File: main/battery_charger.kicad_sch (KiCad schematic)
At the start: 52 parts, among them Q1601 IXTP28P065T, Q1602 TK4R3E06PL, Q1603 IRLML0030, Q1604 FDS6681Z, Q1605 FDS6681Z, Q1606 IRLML0030, U1601 LT8710, U1602 TMCS1101, U1603 TSV911xxLx

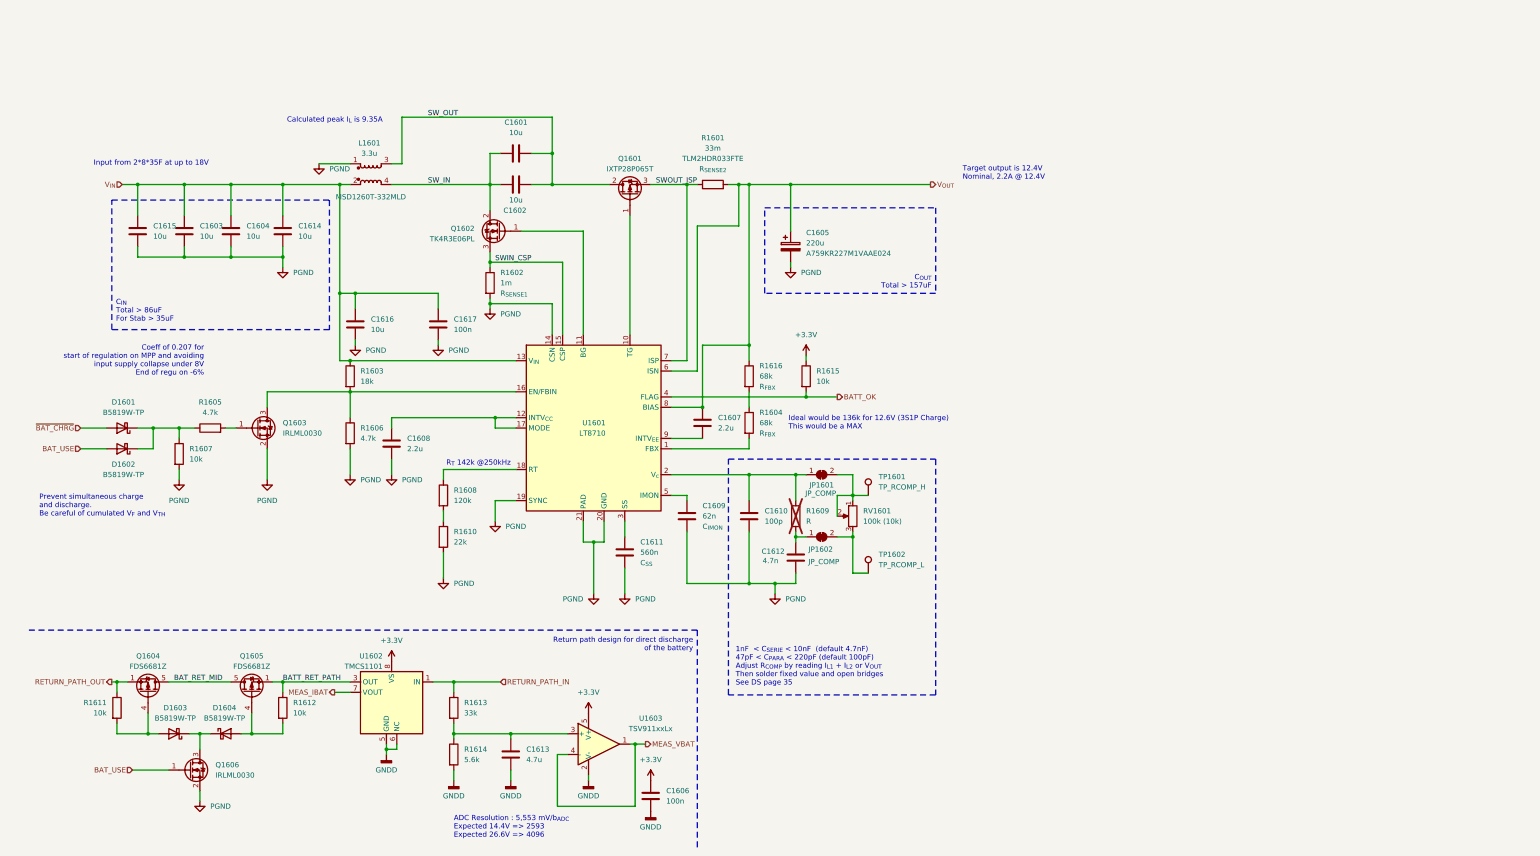
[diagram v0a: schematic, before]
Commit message: Clean silkscreen
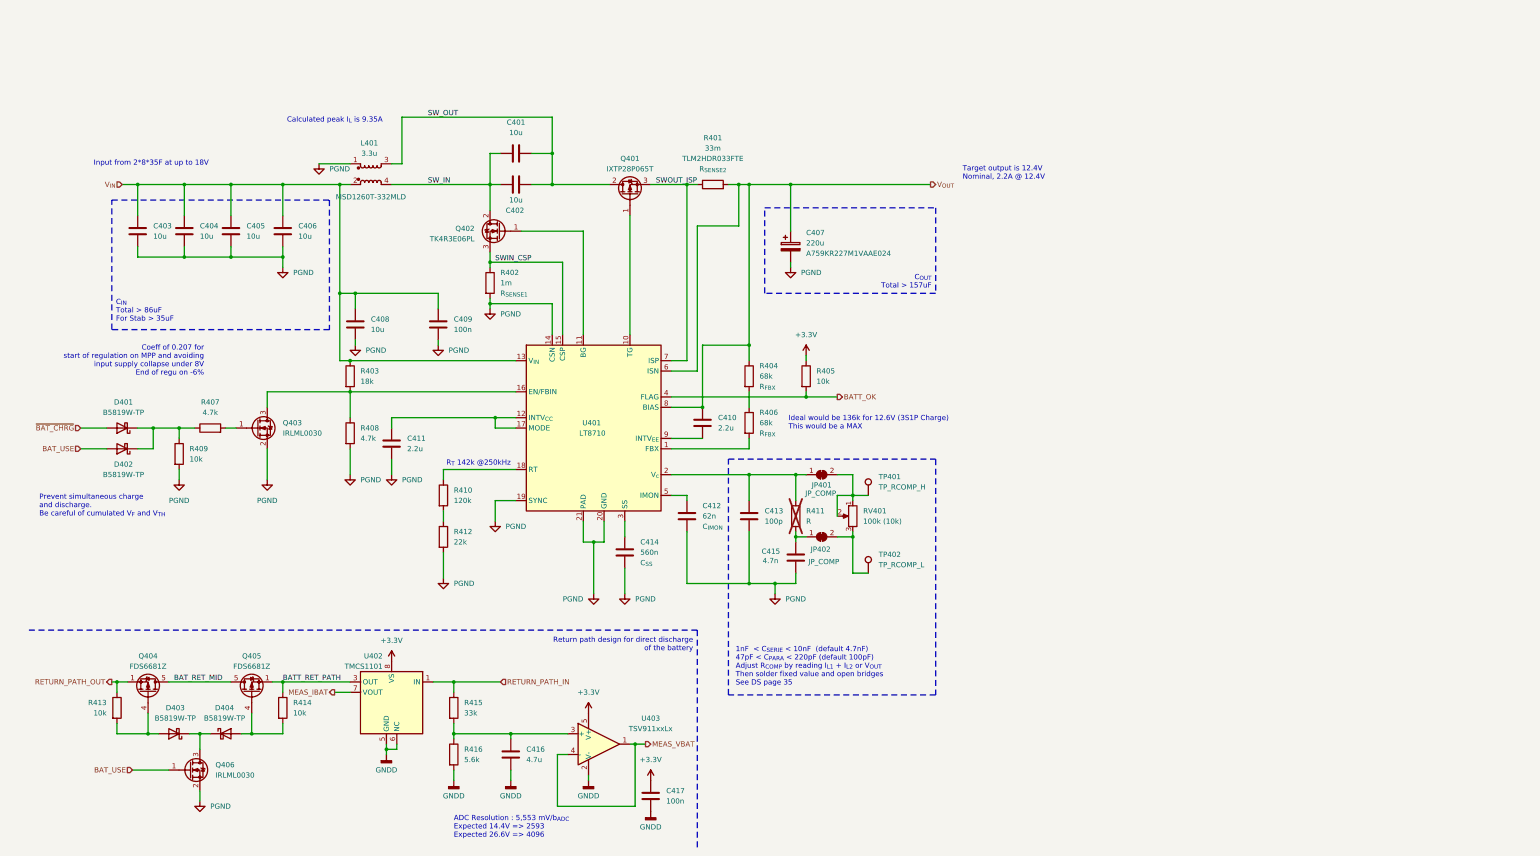
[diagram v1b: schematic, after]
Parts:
- renumbered C1601 to C401, C1602 to C402, C1615 to C403, C1603 to C404, C1604 to C405, C1614 to C406, C1605 to C407, C1616 to C408, C1617 to C409, C1607 to C410, C1608 to C411, C1609 to C412, C1610 to C413, C1611 to C414, C1612 to C415, C1613 to C416, C1606 to C417, D1601 to D401, D1602 to D402, D1603 to D403, D1604 to D404, JP1601 to JP401, JP1602 to JP402, L1601 to L401, Q1601 to Q401, Q1602 to Q402, Q1603 to Q403, Q1604 to Q404, Q1605 to Q405, Q1606 to Q406, R1601 to R401, R1602 to R402, R1603 to R403, R1616 to R404, R1615 to R405, R1604 to R406, R1605 to R407, R1606 to R408, R1607 to R409, R1608 to R410, R1609 to R411, R1610 to R412, R1611 to R413, R1612 to R414, R1613 to R415, R1614 to R416, RV1601 to RV401, TP1601 to TP401, TP1602 to TP402, U1601 to U401, U1602 to U402, U1603 to U403

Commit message: Sent to fab
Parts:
- C401, C402, C403, C404, C405, C406, C408: MPN (none) -> CL21A106KBYQNNE; Mouser SKU (none) -> 187-CL21A106KBYQNNE
- C407: Mouser SKU (none) -> 80-A759KR227M1VAAE24
- C409, C417: MPN (none) -> CL21B104KACNFNC; Mouser SKU (none) -> 187-CL21B104KACNFNC
- C410, C411: MPN (none) -> CL21B225KBYNNWE; Mouser SKU (none) -> 187-CL21B225KBYNNWE
- C412: value 62n -> 68n; MPN (none) -> CL21B683KBCWPNC; Mouser SKU (none) -> 187-CL21B683KBCWPNC
- C413: MPN (none) -> CL21C101JBANNND; Mouser SKU (none) -> 187-CL21C101JBANNND
- C414: value 560n -> 680n; MPN (none) -> CL21B684JOFNNNE; Mouser SKU (none) -> 187-CL21B684JOFNNNE
- C415: MPN (none) -> CL21C472JAFNNNE; Mouser SKU (none) -> 187-CL21C472JAFNNNE
- C416: MPN (none) -> CL21B475KAFNNNE; Mouser SKU (none) -> 187-CL21B475KAFNNNE
- L401: Mouser SKU (none) -> 994-MSD1260T-332MLD
- R401: Mouser SKU (none) -> 279-TLM2HDR033FTE
- R402: MPN (none) -> WSL20101L000FEA18; Mouser SKU (none) -> 71-WSL20101L000FEA18

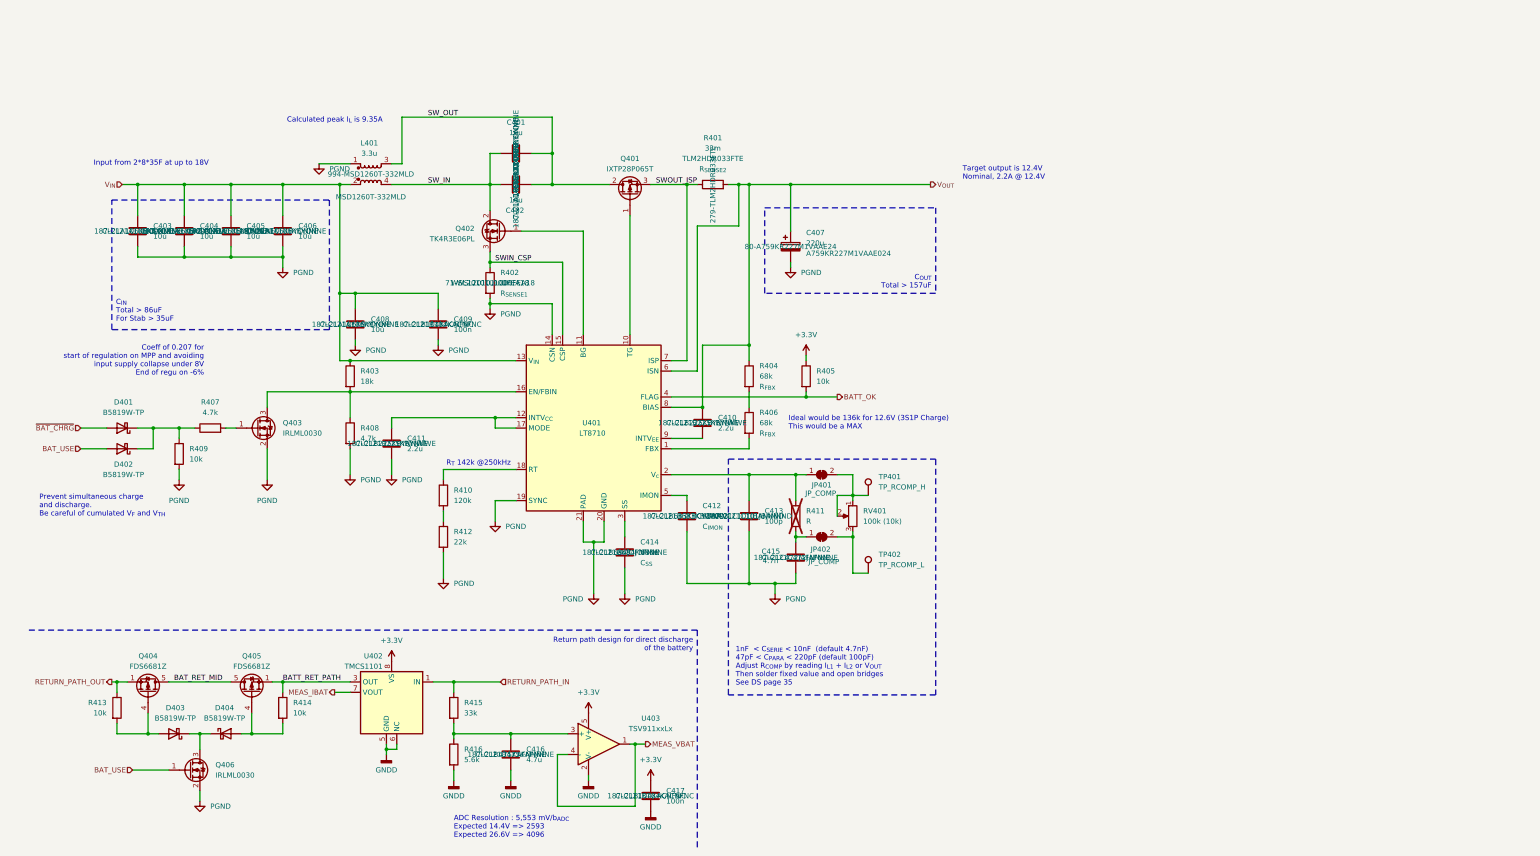
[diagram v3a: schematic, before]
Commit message: BOM almost OK, starts new side board.
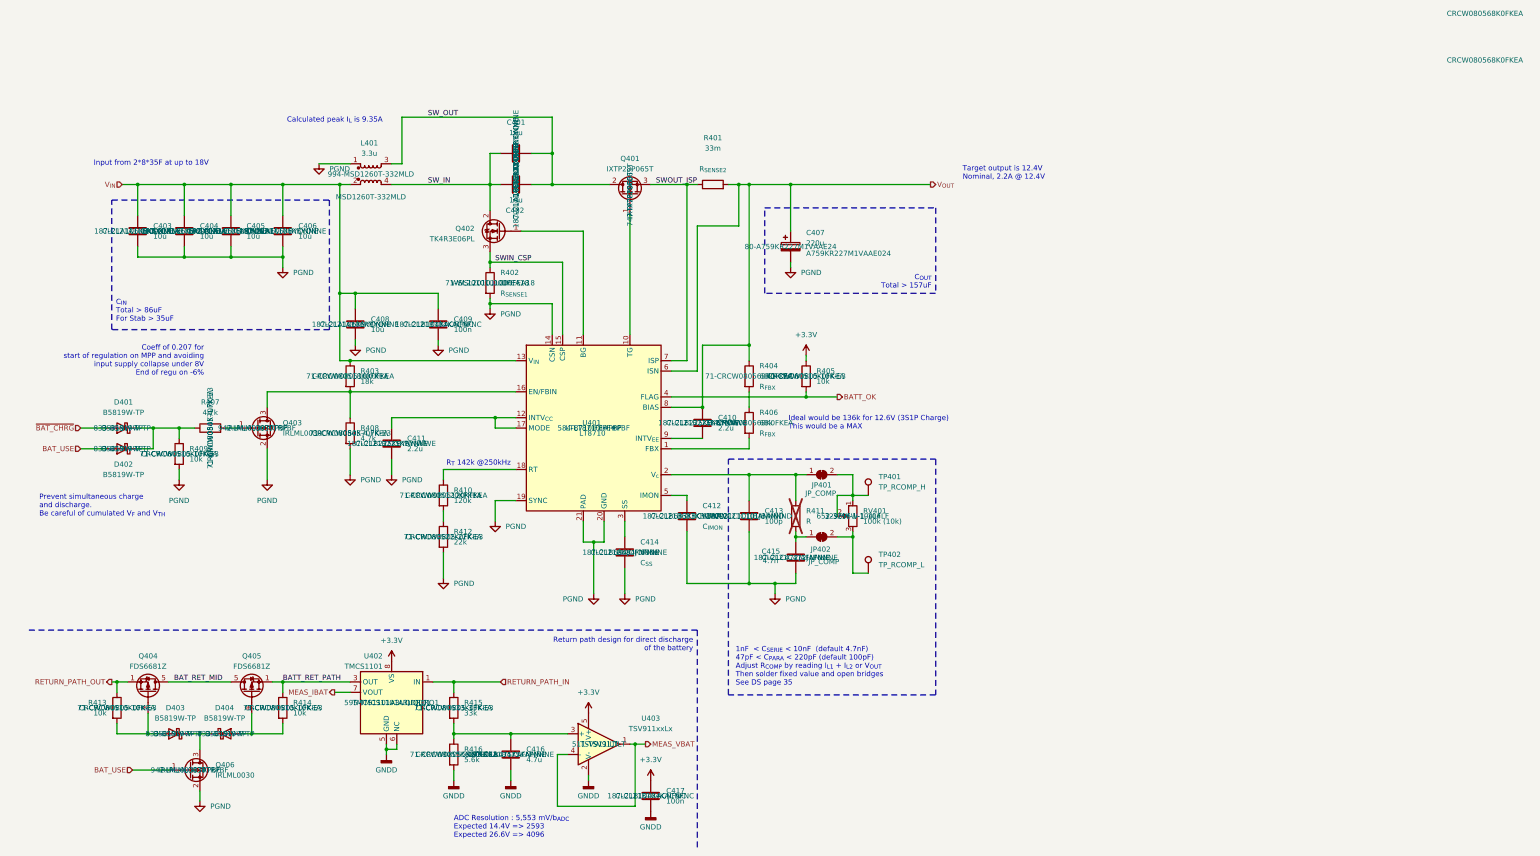
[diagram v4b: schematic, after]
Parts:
- D401, D402, D403, D404: MPN (none) -> B5819W-TP; Mouser SKU (none) -> 833-B5819W-TP
- JP401, JP402: now left out of the parts list
- Q401: MPN (none) -> IXTP28P065T; Mouser SKU (none) -> 747-IXTP28P065T
- Q403, Q406: MPN (none) -> IRLML0030TRPBF; Mouser SKU (none) -> 942-IRLML0030TRPBF
- R401: MPN TLM2HDR033FTE -> (none); Mouser SKU 279-TLM2HDR033FTE -> (none)
- R403: MPN (none) -> CRCW080518K0FKEA; Mouser SKU (none) -> 71-CRCW080518K0FKEA
- R404, R406: MPN (none) -> CRCW080568K0FKEA; Mouser SKU (none) -> 71-CRCW080568K0FKEA
- R405, R409, R413, R414: MPN (none) -> CRCW080510K0FKEA; Mouser SKU (none) -> 71-CRCW0805-10K-E3
- R407, R408: MPN (none) -> CRCW08054K70FKEA; Mouser SKU (none) -> 71-CRCW0805-4.7K-E3
- R410: MPN (none) -> CRCW0805120KFKEA; Mouser SKU (none) -> 71-CRCW0805120KFKEA
- R412: MPN (none) -> CRCW080522K0FKEA; Mouser SKU (none) -> 71-CRCW0805-22K-E3
- R415: MPN (none) -> CRCW080533K0FKEA; Mouser SKU (none) -> 71-CRCW0805-33K-E3
- R416: MPN (none) -> CRCW08055K60FKEA; Mouser SKU (none) -> 71-CRCW08055K60FKEA
- RV401: MPN (none) -> 3296W-1-104LF; Mouser SKU (none) -> 652-3296W-1-104LF
- U401: MPN (none) -> LT8710IFE#PBF; Mouser SKU (none) -> 584-LT8710IFE#PBF
- U402: MPN (none) -> TMCS1101A3UQDRQ1; Mouser SKU (none) -> 595-TMCS1101A3UQDRQ1
- U403: MPN (none) -> TSV911ILT; Mouser SKU (none) -> 511-TSV911ILT

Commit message: Revised with BOM ordered
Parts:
- C401, C402, C403, C404, C405, C406, C408: Mouser SKU 187-CL21A106KBYQNNE -> 187-CL21A106KBYQNNE
- C407: Mouser SKU 80-A759KR227M1VAAE24 -> 80-A759KR227M1VAAE24
- C409, C417: Mouser SKU 187-CL21B104KACNFNC -> 187-CL21B104KACNFNC
- C410, C411: Mouser SKU 187-CL21B225KBYNNWE -> 187-CL21B225KBYNNWE
- C412: Mouser SKU 187-CL21B683KBCWPNC -> 187-CL21B683KBCWPNC
- C413: Mouser SKU 187-CL21C101JBANNND -> 187-CL21C101JBANNND
- C414: Mouser SKU 187-CL21B684JOFNNNE -> 187-CL21B684JOFNNNE
- C415: Mouser SKU 187-CL21C472JAFNNNE -> 187-CL21C472JAFNNNE
- C416: Mouser SKU 187-CL21B475KAFNNNE -> 187-CL21B475KAFNNNE
- L401: value 3.3u -> 4.7u; MPN MSD1260T-332MLD -> MSD1260T-472MLD; Mouser SKU 994-MSD1260T-332MLD -> 994-MSD1260T-472MLD
- Q404, Q405: MPN (none) -> FDS6681Z; Mouser SKU (none) -> 512-FDS6681Z
- R401: value 33m -> 18m; MPN (none) -> WSL2010R0180FEA; Mouser SKU (none) -> 71-WSL2010R0180FEA
- R402: value 1m -> 6m; Mouser SKU 71-WSL20101L000FEA18 -> 71-WSL20101L000FEA18
- R404, R406: MPN CRCW080568K0FKEA -> CRCW080568K0FKEAC; Mouser SKU 71-CRCW080568K0FKEA -> 71-CRCW080568K0FKEAC
- U401: MPN LT8710IFE#PBF -> LT8710IFE#PBF
- U402: MPN TMCS1101A3UQDRQ1 -> TMCS1101A3UQDRQ1
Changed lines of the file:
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@@
 			)
 		)
-		(property "Mouser SKU" " 187-CL21B684JOFNNNE "
+		(property "Mouser SKU" "187-CL21B684JOFNNNE "
 			(at 157.48 124.46 0)
 			(effects
@@
 			)
 		)
+		(property "MPN" "FDS6681Z"
+			(at 66.04 158.75 0)
+			(effects
+				(font
+					(size 1.27 1.27)
+				)
+			)
+		)
+		(property "Mouser SKU" "512-FDS6681Z "
+			(at 66.04 158.75 0)
+			(effects
+				(font
+					(size 1.27 1.27)
+				)
+			)
+		)
 		(pin "6"
 		)
@@
 			)
 		)
-		(property "Mouser SKU" " 187-CL21A106KBYQNNE "
+		(property "Mouser SKU" "187-CL21A106KBYQNNE "
 			(at 130.81 26.67 0)
 			(effects
@@
 			)
 		)
-		(property "Mouser SKU" " 187-CL21A106KBYQNNE "
+		(property "Mouser SKU" "187-CL21A106KBYQNNE "
 			(at 60.96 45.72 0)
 			(effects
@@
 			)
 		)
-		(property "Mouser SKU" " 187-CL21B225KBYNNWE "
+		(property "Mouser SKU" "187-CL21B225KBYNNWE "
 			(at 176.53 92.71 0)
 			(effects
@@
 			)
 		)
-		(property "Value" "3.3u"
+		(property "Value" "4.7u"
 			(at 94.869 26.67 0)
 			(effects
@@
 			)
 		)
-		(property "MPN" " MSD1260T-332MLD "
+		(property "MPN" "MSD1260T-472MLD"
 			(at 95.25 37.338 0)
 			(effects
@@
 			)
 		)
-		(property "Mouser SKU" " 994-MSD1260T-332MLD "
+		(property "Mouser SKU" "994-MSD1260T-472MLD"
+			(at 95.25 31.75 0)
+			(effects
+				(font
+					(size 1.27 1.27)
+				)
+			)
+		)
+		(property "Name" ""
 			(at 95.25 31.75 0)
 			(effects
@@
 		(fields_autoplaced yes)
 		(property "Reference" "R402"
-			(at 127 55.8799 0)
+			(at 127 53.3399 0)
 			(effects
 				(font
@@
 			)
 		)
-		(property "Value" "1m"
-			(at 127 58.4199 0)
+		(property "Value" "6m"
+			(at 127 55.8799 0)
 			(effects
 				(font
@@
 		)
 		(property "MPN" "WSL20101L000FEA18"
-			(at 124.46 58.42 0)
+			(at 127 58.4199 0)
 			(effects
 				(font
 					(size 1.27 1.27)
 				)
+				(justify left)
 			)
 		)
@@
 			)
 		)
-		(property "Mouser SKU" " 71-WSL20101L000FEA18 "
-			(at 124.46 58.42 0)
+		(property "Mouser SKU" "71-WSL20101L000FEA18 "
+			(at 127 63.4999 0)
 			(effects
 				(font
 					(size 1.27 1.27)
 				)
+				(justify left)
 			)
 		)
@@
 			)
 		)
-		(property "MPN" " LT8710IFE#PBF "
+		(property "MPN" "LT8710IFE#PBF "
 			(at 149.86 93.98 0)
 			(effects
@@
 			)
 		)
-		(property "Mouser SKU" " 187-CL21A106KBYQNNE "
+		(property "Mouser SKU" "187-CL21A106KBYQNNE "
 			(at 91.44 68.58 0)
 			(effects
@@
 			)
 		)
-		(property "Mouser SKU" " 187-CL21C101JBANNND "
+		(property "Mouser SKU" "187-CL21C101JBANNND "
 			(at 187.96 115.57 0)
 			(effects
@@
 			)
 		)
-		(property "Mouser SKU" " 187-CL21A106KBYQNNE "
+		(property "Mouser SKU" "187-CL21A106KBYQNNE "
 			(at 49.53 45.72 0)
 			(effects
@@
 			)
 		)
-		(property "Mouser SKU" " 187-CL21B683KBCWPNC "
+		(property "Mouser SKU" "187-CL21B683KBCWPNC "
 			(at 172.72 115.57 0)
 			(effects
@@
 			)
 		)
-		(property "Mouser SKU" " 187-CL21A106KBYQNNE "
+		(property "Mouser SKU" "187-CL21A106KBYQNNE "
 			(at 130.81 34.29 0)
 			(effects
@@
 			)
 		)
-		(property "Mouser SKU" " 187-CL21C472JAFNNNE "
+		(property "Mouser SKU" "187-CL21C472JAFNNNE "
 			(at 199.39 125.73 0)
 			(effects
@@
 			)
 		)
-		(property "Mouser SKU" " 187-CL21B475KAFNNNE "
+		(property "Mouser SKU" "187-CL21B475KAFNNNE "
 			(at 129.54 173.99 0)
 			(effects
@@
 			)
 		)
-		(property "Mouser SKU" " 187-CL21B104KACNFNC "
+		(property "Mouser SKU" "187-CL21B104KACNFNC "
 			(at 163.83 184.15 0)
 			(effects
@@
 			)
 		)
-		(property "Mouser SKU" " 187-CL21B104KACNFNC "
+		(property "Mouser SKU" "187-CL21B104KACNFNC "
 			(at 111.76 68.58 0)
 			(effects
@@
 		(fields_autoplaced yes)
 		(property "Reference" "R401"
-			(at 179.07 22.86 90)
+			(at 179.07 25.4 90)
 			(effects
 				(font
@@
 			)
 		)
-		(property "Value" "33m"
-			(at 179.07 25.4 90)
+		(property "Value" "18m"
+			(at 179.07 27.94 90)
 			(effects
 				(font
@@
 			)
 		)
-		(property "MPN" ""
+		(property "MPN" "WSL2010R0180FEA"
 			(at 179.07 27.94 90)
 			(effects
@@
 			)
 		)
-		(property "Mouser SKU" ""
+		(property "Mouser SKU" "71-WSL2010R0180FEA"
 			(at 179.07 34.29 0)
 			(effects
@@
 			)
 		)
-		(property "MPN" " TMCS1101A3UQDRQ1 "
+		(property "MPN" "TMCS1101A3UQDRQ1 "
 			(at 100.33 161.29 0)
 			(effects
@@
 			)
 		)
-		(property "Mouser SKU" " 80-A759KR227M1VAAE24 "
+		(property "Mouser SKU" "80-A759KR227M1VAAE24 "
 			(at 198.12 49.53 0)
 			(effects
@@
 			)
 		)
-		(property "Mouser SKU" " 187-CL21A106KBYQNNE "
+		(property "Mouser SKU" "187-CL21A106KBYQNNE "
 			(at 38.1 45.72 0)
 			(effects
@@
 			)
 		)
-		(property "Mouser SKU" " 187-CL21A106KBYQNNE "
+		(property "Mouser SKU" "187-CL21A106KBYQNNE "
 			(at 73.66 45.72 0)
 			(effects
@@
 			)
 		)
-		(property "Mouser SKU" " 187-CL21B225KBYNNWE "
+		(property "Mouser SKU" "187-CL21B225KBYNNWE "
 			(at 100.33 97.79 0)
 			(effects
@@
 			)
 		)
-		(property "MPN" "CRCW080568K0FKEA"
+		(property "MPN" "CRCW080568K0FKEAC"
 			(at 368.3 -7.62 0)
 			(effects
@@
 			)
 		)
-		(property "Mouser SKU" " 71-CRCW080568K0FKEA "
+		(property "Mouser SKU" " 71-CRCW080568K0FKEAC"
 			(at 187.96 81.28 0)
 			(effects
@@
 			)
 		)
-		(property "MPN" "CRCW080568K0FKEA"
+		(property "MPN" "CRCW080568K0FKEAC"
 			(at 368.3 3.81 0)
 			(effects
@@
 			)
 		)
-		(property "Mouser SKU" " 71-CRCW080568K0FKEA "
+		(property "Mouser SKU" " 71-CRCW080568K0FKEAC"
 			(at 187.96 92.71 0)
 			(effects
@@
 			)
 		)
+		(property "MPN" "FDS6681Z"
+			(at 40.64 158.75 0)
+			(effects
+				(font
+					(size 1.27 1.27)
+				)
+			)
+		)
+		(property "Mouser SKU" "512-FDS6681Z "
+			(at 40.64 158.75 0)
+			(effects
+				(font
+					(size 1.27 1.27)
+				)
+			)
+		)
 		(pin "6"
 		)
@@
 		(fields_autoplaced yes)
 		(property "Reference" "Q401"
-			(at 158.75 27.94 90)
+			(at 158.75 22.86 90)
 			(effects
 				(font
@@
 		)
 		(property "Value" "IXTP28P065T"
-			(at 158.75 30.48 90)
+			(at 158.75 25.4 90)
 			(effects
 				(font
@@
 		)
 		(property "MPN" " IXTP28P065T "
-			(at 158.75 36.83 0)
+			(at 158.75 27.94 90)
 			(effects
 				(font
@@
 		)
 		(property "Mouser SKU" "747-IXTP28P065T "
-			(at 158.75 36.83 0)
+			(at 158.75 30.48 90)
 			(effects
 				(font
